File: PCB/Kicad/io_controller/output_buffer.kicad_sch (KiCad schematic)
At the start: 8 parts, among them U3 74LS245, U4 74LS245, U5 74LS245, U6 74LS245

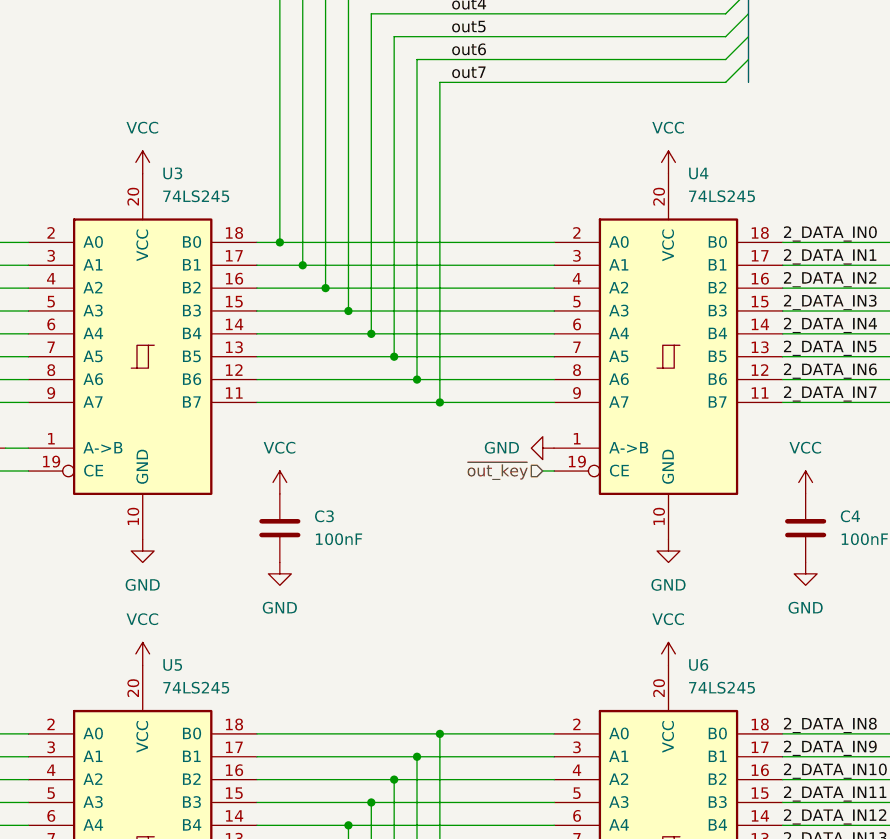
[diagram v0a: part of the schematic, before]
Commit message: io controller WIP ; simulated timer ; adjusted decoder ; adjusted LEDs
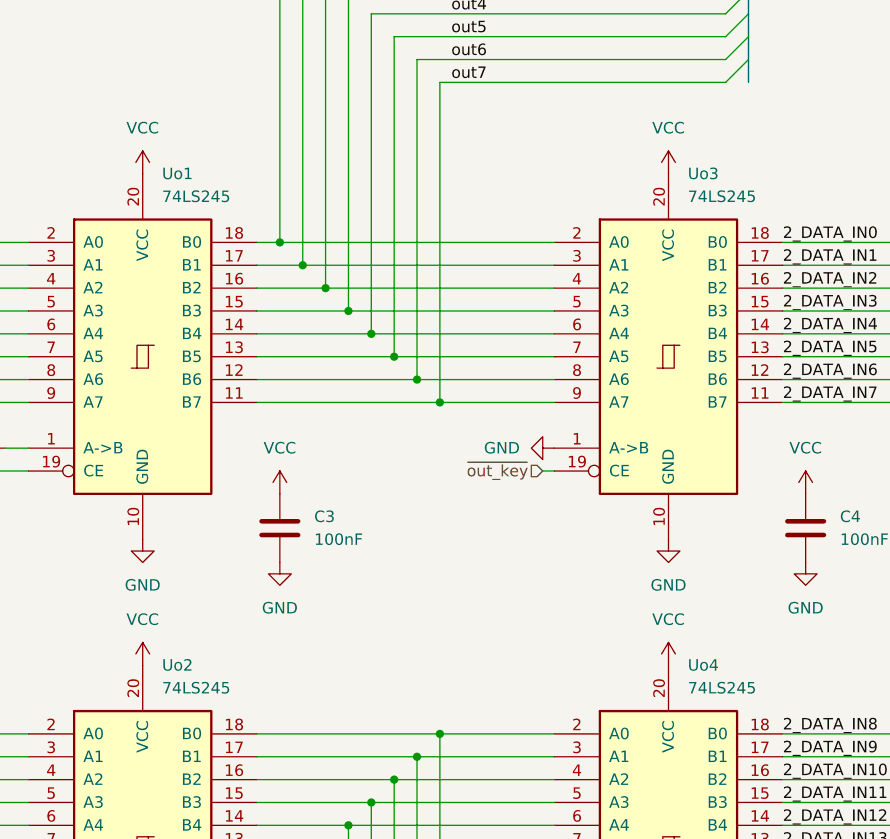
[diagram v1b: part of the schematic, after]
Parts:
- renumbered U3 to Uo1, U5 to Uo2, U4 to Uo3, U6 to Uo4
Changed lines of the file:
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@@
 		(on_board yes)
 		(dnp no)
-		(property "Reference" "U6"
+		(property "Reference" "Uo4"
 			(at 171.0533 104.14 0)
 			(effects
@@
 			(project "io_controller"
 				(path "/dccec861-b967-466c-843e-d6d1ad6064ce/fba438e3-72b6-4de1-833f-e4b9f3f1d00d"
-					(reference "U6")
+					(reference "Uo4")
 					(unit 1)
 				)
@@
 		(on_board yes)
 		(dnp no)
-		(property "Reference" "U4"
+		(property "Reference" "Uo3"
 			(at 171.0533 49.53 0)
 			(effects
@@
 			(project "io_controller"
 				(path "/dccec861-b967-466c-843e-d6d1ad6064ce/fba438e3-72b6-4de1-833f-e4b9f3f1d00d"
-					(reference "U4")
+					(reference "Uo3")
 					(unit 1)
 				)
@@
 		(dnp no)
 		(fields_autoplaced yes)
-		(property "Reference" "U5"
+		(property "Reference" "Uo2"
 			(at 112.6333 104.14 0)
 			(effects
@@
 			(project "io_controller"
 				(path "/dccec861-b967-466c-843e-d6d1ad6064ce/fba438e3-72b6-4de1-833f-e4b9f3f1d00d"
-					(reference "U5")
+					(reference "Uo2")
 					(unit 1)
 				)
@@
 		(dnp no)
 		(fields_autoplaced yes)
-		(property "Reference" "U3"
+		(property "Reference" "Uo1"
 			(at 112.6333 49.53 0)
 			(effects
@@
 			(project "io_controller"
 				(path "/dccec861-b967-466c-843e-d6d1ad6064ce/fba438e3-72b6-4de1-833f-e4b9f3f1d00d"
-					(reference "U3")
-					(unit 1)
-				)
+					(reference "Uo1")
+					(unit 1)
+				)

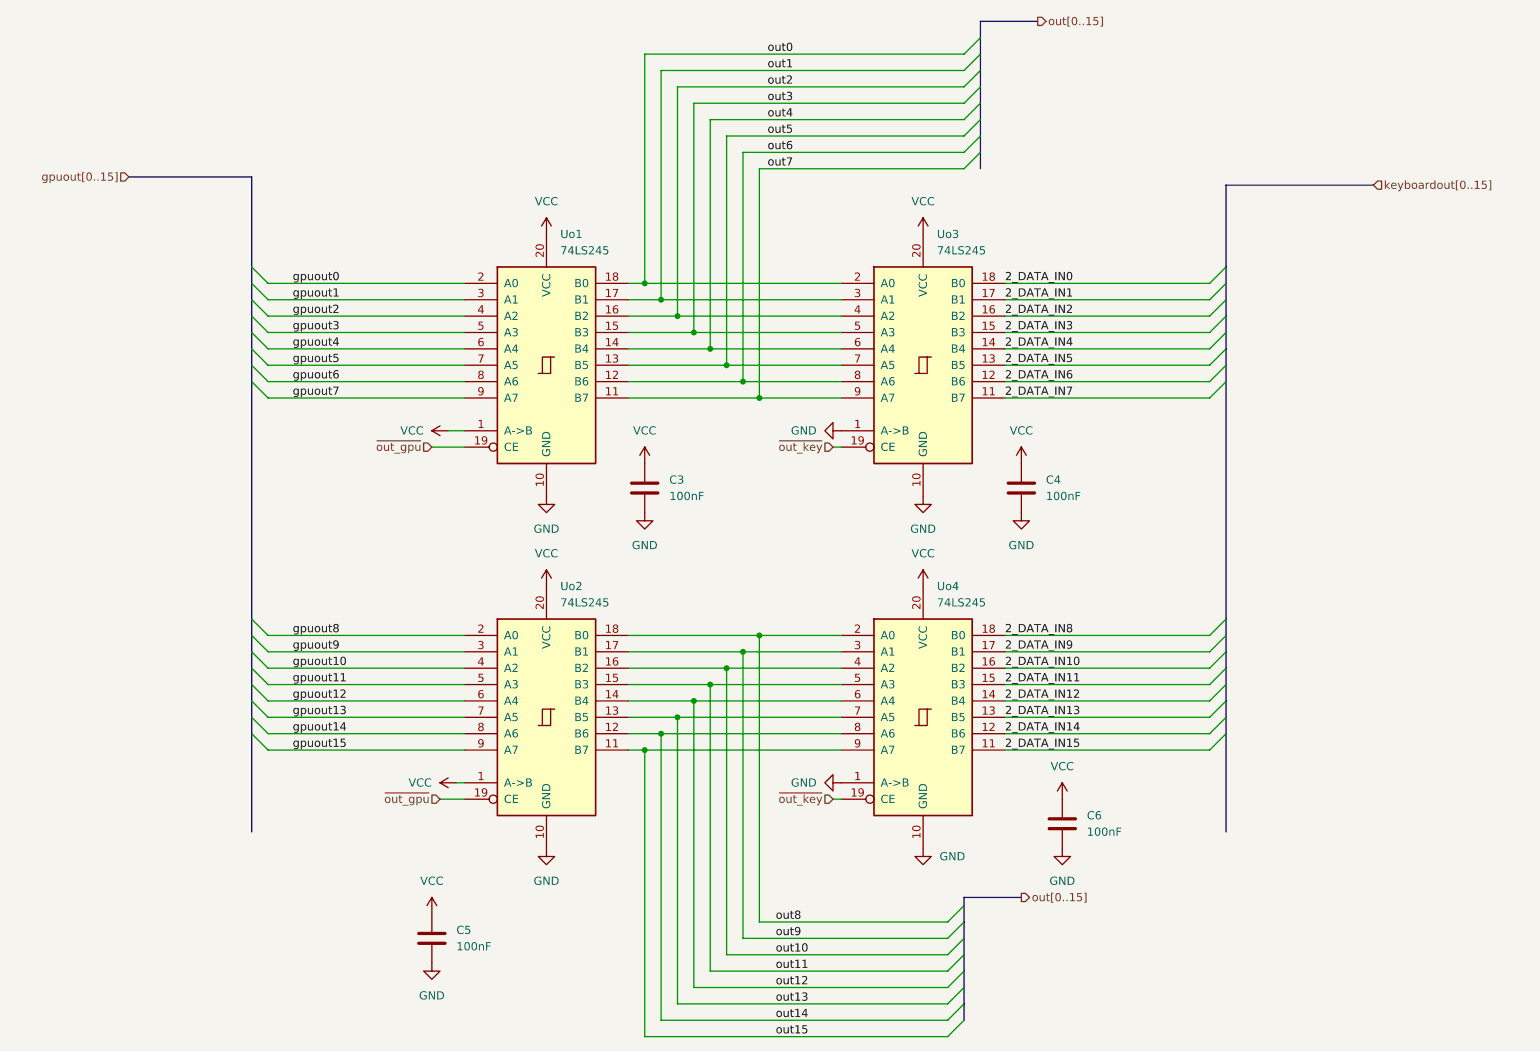
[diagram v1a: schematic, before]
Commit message: more spice models and bugfixes ; more tests of io_controller - mostly keyboard
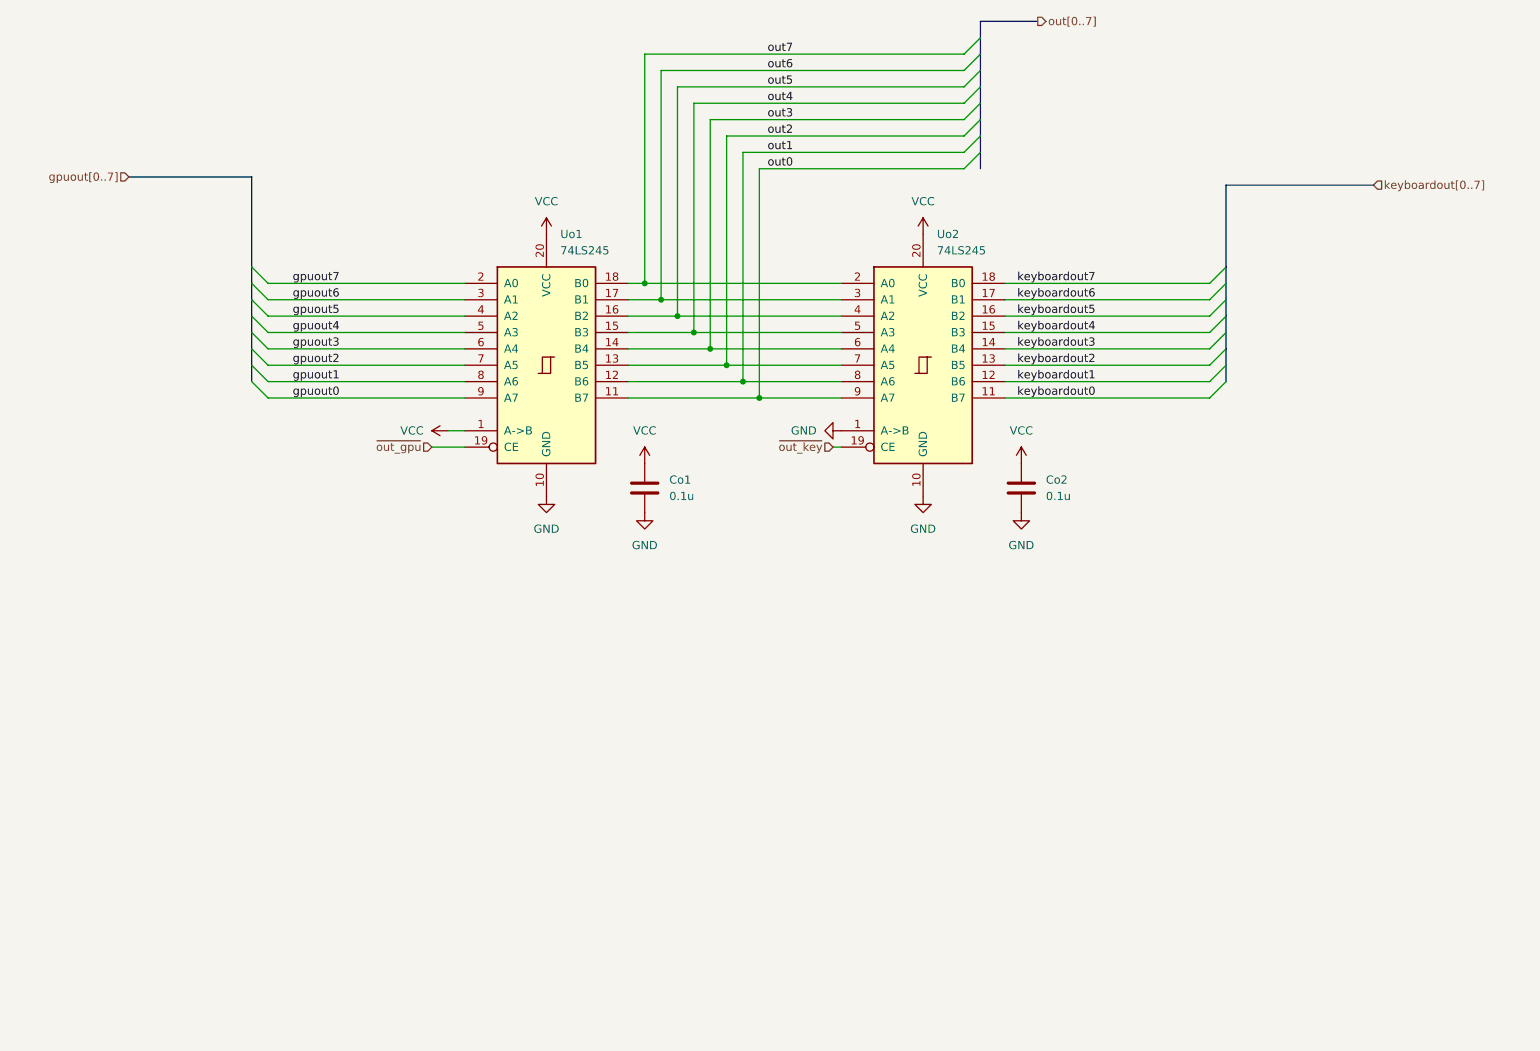
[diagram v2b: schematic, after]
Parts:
- removed C5, C6: 100nF, symbol Device:C
- removed Uo2, Uo4: 74LS245, symbol 74xx:74LS245
- Co1: renamed from C3; value 100nF -> 0.1u; footprint (none) -> Capacitor_SMD:C_0402_1005Metric
- Co2: renamed from C4; value 100nF -> 0.1u; footprint (none) -> Capacitor_SMD:C_0402_1005Metric
- Uo1: footprint (none) -> Package_SO:SOIC-20W_7.5x12.8mm_P1.27mm
- Uo2: renamed from Uo3; footprint (none) -> Package_SO:SOIC-20W_7.5x12.8mm_P1.27mm
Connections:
- net gpuout0: now also Uo1.9 (A7); no longer Uo1.2 (A0)
- net gpuout1: now also Uo1.8 (A6); no longer Uo1.3 (A1)
- net gpuout2: now also Uo1.7 (A5); no longer Uo1.4 (A2)
- net gpuout3: now also Uo1.6 (A4); no longer Uo1.5 (A3)
- net gpuout4: now also Uo1.5 (A3); no longer Uo1.6 (A4)
- net gpuout5: now also Uo1.4 (A2); no longer Uo1.7 (A5)
- net gpuout6: now also Uo1.3 (A1); no longer Uo1.8 (A6)
- net gpuout7: now also Uo1.2 (A0); no longer Uo1.9 (A7)
- net out0: now also Uo1.11 (B7), Uo2.9 (A7); no longer Uo1.18 (B0), Uo2.2 (A0)
- net out1: now also Uo1.12 (B6), Uo2.8 (A6); no longer Uo1.17 (B1), Uo2.3 (A1)
- net out2: now also Uo1.13 (B5), Uo2.7 (A5); no longer Uo1.16 (B2), Uo2.4 (A2)
- net out3: now also Uo1.14 (B4), Uo2.6 (A4); no longer Uo1.15 (B3), Uo2.5 (A3)
- net out4: now also Uo1.15 (B3), Uo2.5 (A3); no longer Uo1.14 (B4), Uo2.6 (A4)
- net out5: now also Uo1.16 (B2), Uo2.4 (A2); no longer Uo1.13 (B5), Uo2.7 (A5)
- net out6: now also Uo1.17 (B1), Uo2.3 (A1); no longer Uo1.12 (B6), Uo2.8 (A6)
- net out7: now also Uo1.18 (B0), Uo2.2 (A0); no longer Uo1.11 (B7), Uo2.9 (A7)
- net 2_DATA_IN0 renamed keyboardout7
- net 2_DATA_IN1 renamed keyboardout6
- net 2_DATA_IN2 renamed keyboardout5
- net 2_DATA_IN3 renamed keyboardout4
- net 2_DATA_IN4 renamed keyboardout3
- net 2_DATA_IN5 renamed keyboardout2
- net 2_DATA_IN6 renamed keyboardout1
- net 2_DATA_IN7 renamed keyboardout0
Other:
- company: (none) -> AGH Logic Unit
- title: (none) -> Output Buffer

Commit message: primarily keyboard decoder finish ; preliminary layout
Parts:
- added Ro1, Ro2, Ro3, Ro4, Ro5, Ro6, Ro7, Ro8: 10k, Resistor_SMD:R_0402_1005Metric, symbol Device:R
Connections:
- net GND: now also Ro1.2, Ro2.2, Ro3.2, Ro4.2, Ro5.2, Ro6.2, Ro7.2, Ro8.2
- net out0: now also Ro8.1
- net out1: now also Ro7.1
- net out2: now also Ro6.1
- net out3: now also Ro5.1
- net out4: now also Ro4.1
- net out5: now also Ro3.1
- net out6: now also Ro2.1
- net out7: now also Ro1.1
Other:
- note added: "Ro1 to Ro7 10k"
- moved on the sheet: Co1
